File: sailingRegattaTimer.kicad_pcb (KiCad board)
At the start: 2 copper layers, 25 parts, among them J1-Red-1M1 Conn_01x02_Socket, J10-12v-In1 Conn_01x02_Socket, J2-Yel-2M1 Conn_01x02_Socket, J3-Grn-3M1 J3-Grn-3M, J4-Blu-5M1 J4-Blu-5M1, J5-5v-LED1 Conn_01x02_Socket, J6-Reset1 J6-Reset, J7-Ext-Buz1 Conn_01x02_Socket, J8-Pololu-VReg1 Conn_01x04_Socket, J9-Relay1 Conn_01x03_Socket

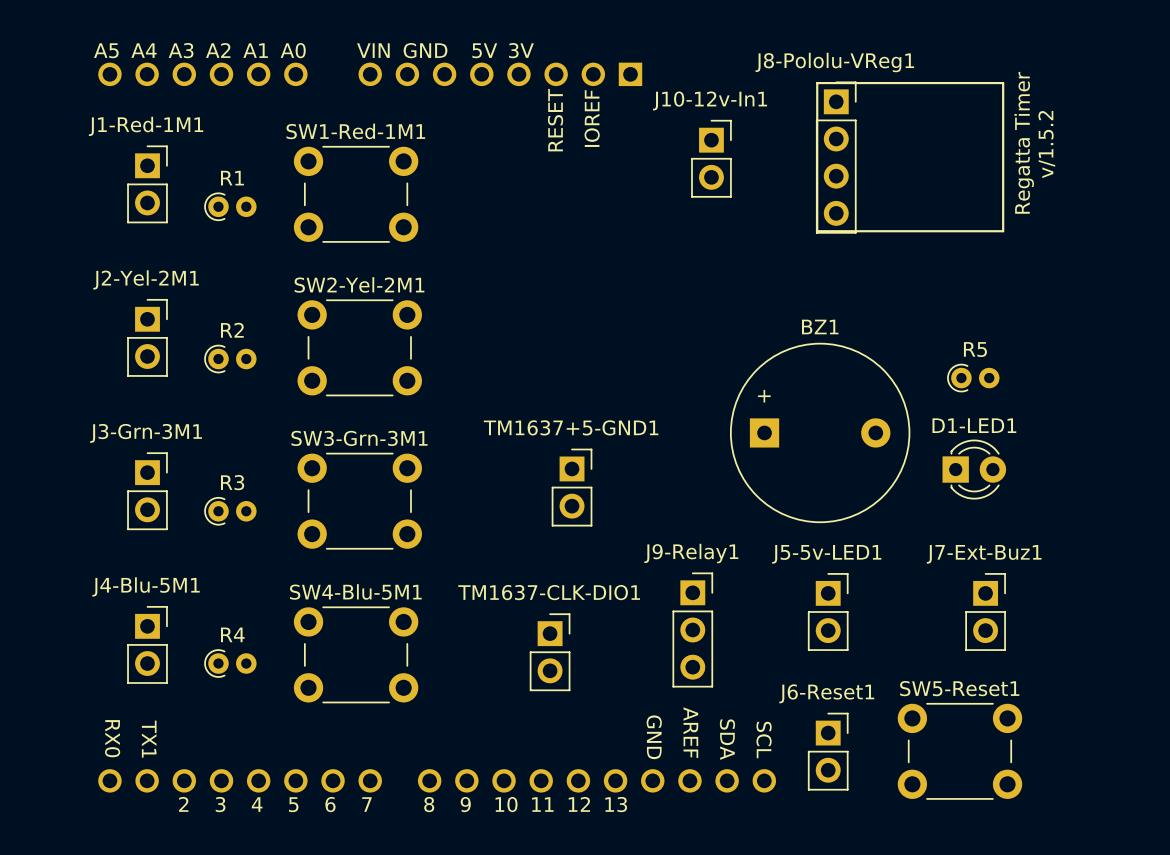
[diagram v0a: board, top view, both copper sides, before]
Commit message: completed pcb layout
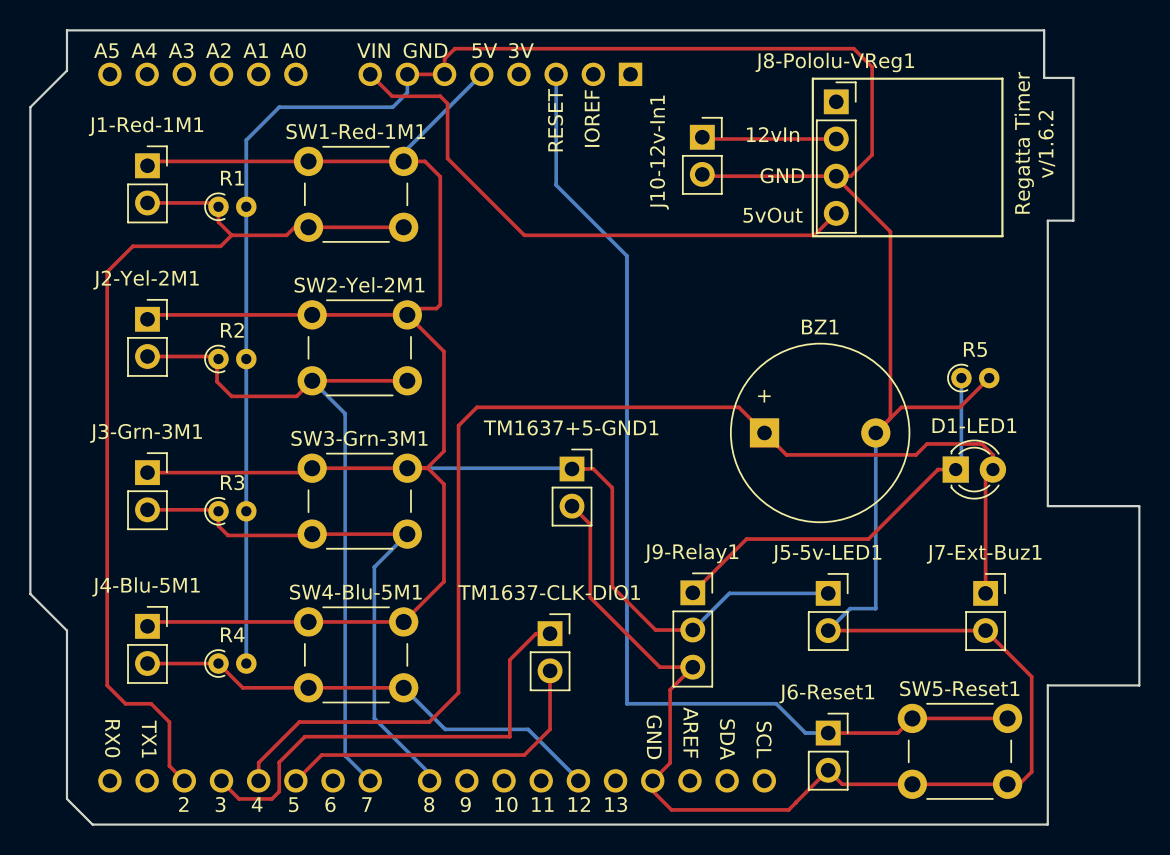
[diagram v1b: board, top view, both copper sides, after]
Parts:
- moved J10-12v-In1 0.66 mm to (188.4, 48.5)
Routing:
- net GND: track 0.00 -> 221.2 mm
- net +5V: track 0.00 -> 158.5 mm
- net Net-(A1-D4): track 0.00 -> 83.8 mm
- net Net-(A1-~{RESET}): track 0.00 -> 72.2 mm
- net Net-(A1-D2): track 0.00 -> 66.8 mm
- net Net-(A1-D7): track 0.00 -> 49.3 mm
- net Net-(A1-VIN): track 0.00 -> 39.2 mm
- net Net-(A1-D8): track 0.00 -> 38.4 mm
- net Net-(A1-D12): track 0.00 -> 32.8 mm
- net Net-(A1-D3): track 0.00 -> 31.9 mm
- net Net-(D1-LED1-K): track 0.00 -> 27.9 mm
- net Net-(A1-D5): track 0.00 -> 22.8 mm
- net Net-(J10-12v-In1-Pin_1): track 0.00 -> 9.20 mm
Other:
- board outline added: 75.8 x 54.2 mm
- board text added: "12vIn"
- board text added: "5vOut"
- board text added: "GND"
- board text added: "Regatta Timer v/1.6.2"
- board text removed: "Regatta Timer v/1.5.2"

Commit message: initial commit - schematic and pcb
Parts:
- removed R1: R1, Resistor_THT:R_Axial_DIN0204_L3.6mm_D1.6mm_P1.90mm_Vertical
- removed R2, R3, R4: R, Resistor_THT:R_Axial_DIN0204_L3.6mm_D1.6mm_P1.90mm_Vertical
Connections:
- J1-Red-1M1 pad 1: +5V -> GND
- J2-Yel-2M1 pad 1: +5V -> GND
- J3-Grn-3M1 pad 1: +5V -> GND
- J4-Blu-5M1 pad 1: +5V -> GND
- SW1-Red-1M1 pad 1: +5V -> GND
- SW2-Yel-2M1 pad 1: +5V -> GND
- SW3-Grn-3M1 pad 1: +5V -> GND
- SW4-Blu-5M1 pad 1: +5V -> GND
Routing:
- net +5V: track 158.5 -> 56.6 mm
- net GND: track 221.2 -> 269.9 mm
- net Net-(A1-D2): track 66.8 -> 62.5 mm
- net Net-(A1-VIN): track 39.2 -> 35.8 mm
- net Net-(A1-D7): track 49.3 -> 47.4 mm
- net Net-(A1-~{RESET}): track 72.2 -> 71.0 mm
- net Net-(A1-D8): track 38.4 -> 37.9 mm
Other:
- board text added: "Regatta Timer v/2.0.0"
- board text removed: "Regatta Timer v/1.6.2"
